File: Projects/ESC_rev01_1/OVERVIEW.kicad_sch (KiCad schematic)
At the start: 0 parts

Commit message: Update 07
Schematic is ready
INPUT PROTECTION schematic created
MOSFETs schematic created
CAN schematic created
FILTERs schematic created
MECHANICAL schematic created
STEP-DOWN schematic created
Footprints, 3D models are added and corrected (major issues)
Component placement started
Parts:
- added CR1: PUSB3AB6Z, DF_ESC_rev01_1:XSON-7_L2.2-W1.2-P0.50-BL, symbol PUSB3AB6Z:PUSB3AB6Z
- added R56, R57, R58: 0R, Resistor_SMD:R_0603_1608Metric, symbol Device:R
- added R59, R60: 5k1, Resistor_SMD:R_0603_1608Metric, symbol Device:R
- added R61, R62: 22R, Resistor_SMD:R_0603_1608Metric, symbol Device:R
- added U11: TYPE-C-31-M-12, DF_ESC_rev01_1:USB-C_SMD-TYPE-C-31-M-12_1, symbol TYPE-C-31-M-12:TYPE-C-31-M-12
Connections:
- new net: R56.2, R57.2, U11.1 (EH), U11.2 (EH), U11.3 (EH), U11.4 (EH)
- new net +5V: R58.2
- new net +5V-C: CR1.3 (IO2), CR1.5 (IO4), R58.1, U11.A4B9 (VBUS), U11.B4A9 (VBUS)
- new net CC1: CR1.4 (IO3), R60.2, U11.A5 (CC1)
- new net CC2: CR1.1 (IO1), R59.2, U11.B5 (CC2)
- new net GND: CR1.2 (GND), R56.1, R57.1, R59.1, R60.1, U11.A1B12 (GND), U11.B1A12 (GND)
- new net USB-C_N: CR1.6 (IO5), R61.1, U11.A7 (DN1), U11.B7 (DN2)
- new net USB-C_P: CR1.7 (IO6), R62.1, U11.A6 (DP1), U11.B6 (DP2)
- new net USB_N: R61.2
- new net USB_P: R62.2
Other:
- note added: "ESD PROTECTION PLACE AS CLOSE AS POSSIBLE TO THE CONNECTOR"
- note added: "FIT A ZERO OMH LINK, CAP, OR RESISTOR"
- note added: "MOUNT A OR JUMPER IF USED AS USB HOST"
- note added: "PULL-DOWN TELL THE HOST WE ARE UFP. ONLY ONE USED AT GIVEN TIME. BOTH NECESSARY FOR REVERSIBILITY."
- note added: "ROUTE AS DIFFERENTIAL PAIR"
- note added: "TERMINATING RESISTORS PLACE AS CLOSE AS POSSIBLE TO MCU"
- note added: "[09] - USB"

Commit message: Update 09
Components placement finished
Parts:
- renumbered U11 to J11, R56 to R53, R57 to R54, R58 to R55, R59 to R56, R60 to R57, R61 to R58, R62 to R59
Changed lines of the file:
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@@
 		(on_board yes)
 		(dnp no)
-		(property "Reference" "#PWR098"
+		(property "Reference" "#PWR095"
 			(at 100.33 142.24 0)
 			(effects
@@
 			(project "ESC_rev01_1"
 				(path "/e63e39d7-6ac0-4ffd-8aa3-1841a4541b55/aa28b6a5-844a-4eb8-af03-0b1ead627e2c"
-					(reference "#PWR098")
+					(reference "#PWR095")
 					(unit 1)
 				)
@@
 		(on_board yes)
 		(dnp no)
-		(property "Reference" "R58"
+		(property "Reference" "R55"
 			(at 128.778 70.104 0)
 			(effects
@@
 			(project "ESC_rev01_1"
 				(path "/e63e39d7-6ac0-4ffd-8aa3-1841a4541b55/aa28b6a5-844a-4eb8-af03-0b1ead627e2c"
-					(reference "R58")
+					(reference "R55")
 					(unit 1)
 				)
@@
 		(on_board yes)
 		(dnp no)
-		(property "Reference" "R61"
+		(property "Reference" "R58"
 			(at 203.2 71.12 90)
 			(effects
@@
 			(project "ESC_rev01_1"
 				(path "/e63e39d7-6ac0-4ffd-8aa3-1841a4541b55/aa28b6a5-844a-4eb8-af03-0b1ead627e2c"
-					(reference "R61")
+					(reference "R58")
 					(unit 1)
 				)
@@
 		(on_board yes)
 		(dnp no)
-		(property "Reference" "#PWR0102"
+		(property "Reference" "#PWR099"
 			(at 187.96 114.3 0)
 			(effects
@@
 			(project "ESC_rev01_1"
 				(path "/e63e39d7-6ac0-4ffd-8aa3-1841a4541b55/aa28b6a5-844a-4eb8-af03-0b1ead627e2c"
-					(reference "#PWR0102")
+					(reference "#PWR099")
 					(unit 1)
 				)
@@
 		(dnp no)
 		(fields_autoplaced yes)
-		(property "Reference" "U11"
+		(property "Reference" "J11"
 			(at 99.06 71.12 0)
 			(effects
@@
 			(project ""
 				(path "/e63e39d7-6ac0-4ffd-8aa3-1841a4541b55/aa28b6a5-844a-4eb8-af03-0b1ead627e2c"
-					(reference "U11")
+					(reference "J11")
 					(unit 1)
 				)
@@
 		(dnp no)
 		(fields_autoplaced yes)
-		(property "Reference" "#PWR099"
+		(property "Reference" "#PWR096"
 			(at 125.73 62.23 0)
 			(effects
@@
 			(project ""
 				(path "/e63e39d7-6ac0-4ffd-8aa3-1841a4541b55/aa28b6a5-844a-4eb8-af03-0b1ead627e2c"
-					(reference "#PWR099")
+					(reference "#PWR096")
 					(unit 1)
 				)
@@
 		(on_board yes)
 		(dnp no)
-		(property "Reference" "R60"
+		(property "Reference" "R57"
 			(at 151.638 91.694 0)
 			(effects
@@
 			(project "ESC_rev01_1"
 				(path "/e63e39d7-6ac0-4ffd-8aa3-1841a4541b55/aa28b6a5-844a-4eb8-af03-0b1ead627e2c"
-					(reference "R60")
+					(reference "R57")
 					(unit 1)
 				)
@@
 		(on_board yes)
 		(dnp no)
-		(property "Reference" "#PWR0100"
+		(property "Reference" "#PWR097"
 			(at 140.97 106.68 0)
 			(effects
@@
 			(project "ESC_rev01_1"
 				(path "/e63e39d7-6ac0-4ffd-8aa3-1841a4541b55/aa28b6a5-844a-4eb8-af03-0b1ead627e2c"
-					(reference "#PWR0100")
+					(reference "#PWR097")
 					(unit 1)
 				)
@@
 		(on_board yes)
 		(dnp no)
-		(property "Reference" "R59"
+		(property "Reference" "R56"
 			(at 144.018 91.694 0)
 			(effects
@@
 			(project "ESC_rev01_1"
 				(path "/e63e39d7-6ac0-4ffd-8aa3-1841a4541b55/aa28b6a5-844a-4eb8-af03-0b1ead627e2c"
-					(reference "R59")
+					(reference "R56")
 					(unit 1)
 				)
@@
 		(on_board yes)
 		(dnp no)
-		(property "Reference" "R56"
+		(property "Reference" "R53"
 			(at 88.138 124.714 0)
 			(effects
@@
 			(project "ESC_rev01_1"
 				(path "/e63e39d7-6ac0-4ffd-8aa3-1841a4541b55/aa28b6a5-844a-4eb8-af03-0b1ead627e2c"
-					(reference "R56")
+					(reference "R53")
 					(unit 1)
 				)
@@
 		(on_board yes)
 		(dnp no)
-		(property "Reference" "R62"
+		(property "Reference" "R59"
 			(at 203.2 77.47 90)
 			(effects
@@
 			(project "ESC_rev01_1"
 				(path "/e63e39d7-6ac0-4ffd-8aa3-1841a4541b55/aa28b6a5-844a-4eb8-af03-0b1ead627e2c"
-					(reference "R62")
+					(reference "R59")
 					(unit 1)
 				)
@@
 		(on_board yes)
 		(dnp no)
-		(property "Reference" "#PWR0101"
+		(property "Reference" "#PWR098"
 			(at 148.59 106.68 0)
 			(effects
@@
 			(project "ESC_rev01_1"
 				(path "/e63e39d7-6ac0-4ffd-8aa3-1841a4541b55/aa28b6a5-844a-4eb8-af03-0b1ead627e2c"
-					(reference "#PWR0101")
+					(reference "#PWR098")
 					(unit 1)
 				)
@@
 		(on_board yes)
 		(dnp no)
-		(property "Reference" "R57"
+		(property "Reference" "R54"
 			(at 94.488 124.714 0)
 			(effects
@@
 			(project "ESC_rev01_1"
 				(path "/e63e39d7-6ac0-4ffd-8aa3-1841a4541b55/aa28b6a5-844a-4eb8-af03-0b1ead627e2c"
-					(reference "R57")
-					(unit 1)
-				)
+					(reference "R54")
+					(unit 1)
+				)

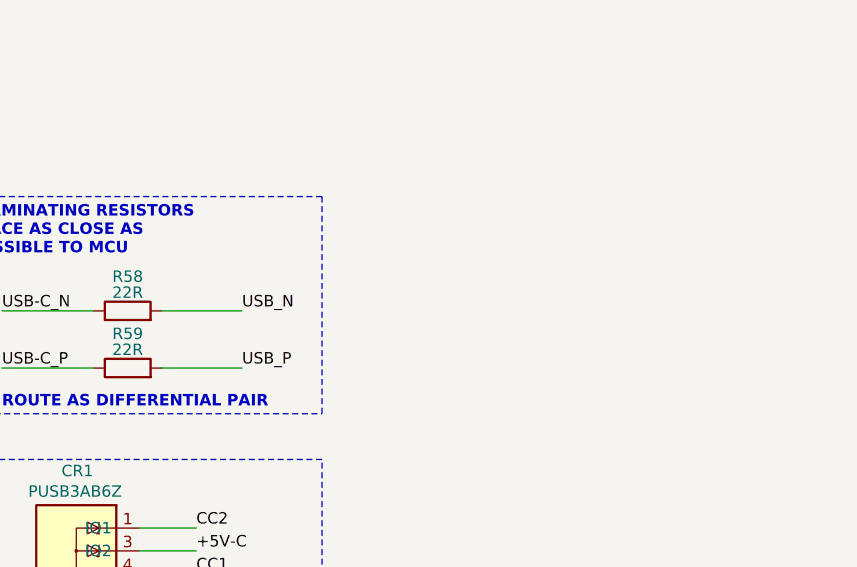
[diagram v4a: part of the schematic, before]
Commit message: Update 11
Draft routing - diff signals and power
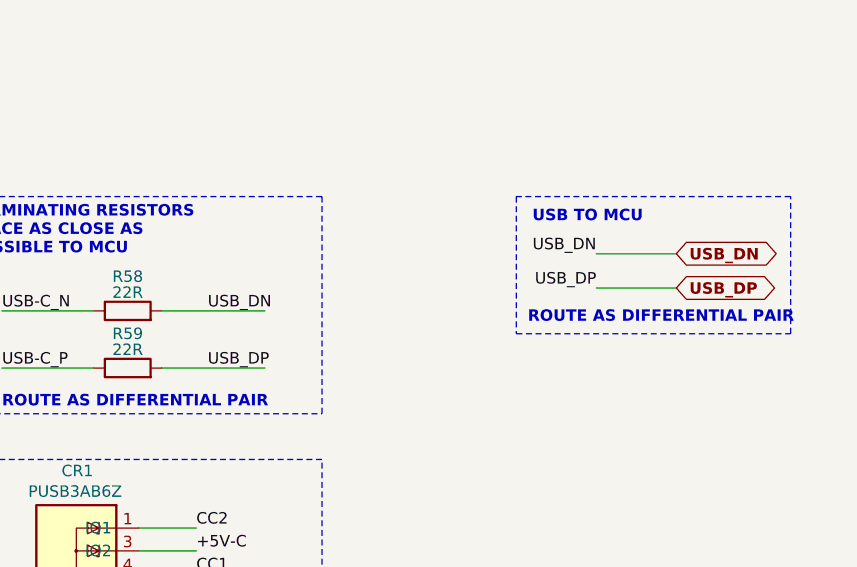
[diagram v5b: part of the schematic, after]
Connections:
- net USB_N renamed USB_DN
- net USB_P renamed USB_DP
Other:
- note added: "USB TO MCU"
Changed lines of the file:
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@@
+		)
+	)
+	(text "ROUTE AS DIFFERENTIAL PAIR"
+		(exclude_from_sim no)
+		(at 247.65 75.692 0)
+		(effects
+			(font
+				(size 1.27 1.27)
+				(thickness 0.254)
+				(bold yes)
+			)
+			(justify left)
 		)
 	)
@@
 		(exclude_from_sim no)
 		(at 100.33 64.77 0)
+		(effects
+			(font
+				(size 1.27 1.27)
+				(thickness 0.254)
+				(bold yes)
+			)
+			(justify left)
+		)
+	)
+	(text "USB TO MCU"
+		(exclude_from_sim no)
+		(at 248.158 64.516 0)
 		(effects
 			(font
@@
 		)
 	)
+	(polyline
+		(pts
+			(xy 246.38 62.23) (xy 246.38 77.47)
+		)
+		(stroke
+			(width 0)
+			(type dash)
+		)
+	)
+	(wire
+		(pts
+			(xy 264.16 68.58) (xy 255.27 68.58)
+		)
+		(stroke
+			(width 0.5)
+			(type default)
+		)
+	)
 	(wire
 		(pts
@@
 		)
 	)
+	(wire
+		(pts
+			(xy 207.01 81.28) (xy 218.44 81.28)
+		)
+		(stroke
+			(width 0.508)
+			(type default)
+		)
+	)
+	(polyline
+		(pts
+			(xy 276.86 77.47) (xy 276.86 62.23)
+		)
+		(stroke
+			(width 0)
+			(type dash)
+		)
+	)
 	(polyline
 		(pts
@@
 		)
 	)
-	(wire
-		(pts
-			(xy 215.9 81.28) (xy 207.01 81.28)
-		)
-		(stroke
-			(width 0.5)
-			(type default)
+	(polyline
+		(pts
+			(xy 246.38 77.47) (xy 276.86 77.47)
+		)
+		(stroke
+			(width 0)
+			(type dash)
 		)
 	)
@@
 	(wire
 		(pts
+			(xy 207.01 74.93) (xy 218.44 74.93)
+		)
+		(stroke
+			(width 0.508)
+			(type default)
+		)
+	)
+	(wire
+		(pts
 			(xy 91.44 133.35) (xy 100.33 133.35)
 		)
@@
 	(wire
 		(pts
+			(xy 264.16 72.39) (xy 255.27 72.39)
+		)
+		(stroke
+			(width 0.5)
+			(type default)
+		)
+	)
+	(wire
+		(pts
 			(xy 100.33 114.3) (xy 102.87 114.3)
 		)
@@
 		)
 	)
-	(wire
-		(pts
-			(xy 207.01 74.93) (xy 215.9 74.93)
-		)
-		(stroke
-			(width 0.5)
-			(type default)
-		)
-	)
 	(polyline
 		(pts
@@
 		)
 		(stroke
-			(width 0.5)
+			(width 0.508)
 			(type default)
 		)
@@
 		)
 		(stroke
-			(width 0.5)
+			(width 0.508)
 			(type default)
 		)
@@
 	(polyline
 		(pts
+			(xy 276.86 62.23) (xy 246.38 62.23)
+		)
+		(stroke
+			(width 0)
+			(type dash)
+		)
+	)
+	(polyline
+		(pts
 			(xy 100.33 68.58) (xy 100.33 60.96)
 		)
@@
 			(width 0)
 			(type default)
+		)
+	)
+	(label "USB_DN"
+		(at 212.09 74.93 0)
+		(effects
+			(font
+				(size 1.27 1.27)
+				(thickness 0.1588)
+			)
+			(justify left bottom)
 		)
 	)
@@
 		)
 	)
-	(label "USB_P"
-		(at 215.9 81.28 0)
-		(effects
-			(font
-				(size 1.27 1.27)
-			)
-			(justify left bottom)
+	(label "USB_DP"
+		(at 255.27 72.39 180)
+		(effects
+			(font
+				(size 1.27 1.27)
+			)
+			(justify right bottom)
 		)
 	)
@@
 		)
 	)
-	(label "USB_N"
-		(at 215.9 74.93 0)
-		(effects
-			(font
-				(size 1.27 1.27)
-			)
-			(justify left bottom)
+	(label "USB_DN"
+		(at 255.27 68.58 180)
+		(effects
+			(font
+				(size 1.27 1.27)
+			)
+			(justify right bottom)
 		)
 	)
@@
 		)
 	)
+	(label "USB_DP"
+		(at 212.09 81.28 0)
+		(effects
+			(font
+				(size 1.27 1.27)
+				(thickness 0.1588)
+			)
+			(justify left bottom)
+		)
+	)
 	(label "+5V-C"
 		(at 210.82 101.6 0)
@@
 		)
 	)
+	(global_label "USB_DP"
+		(shape bidirectional)
+		(at 264.16 72.39 0)
+		(fields_autoplaced yes)
+		(effects
+			(font
+				(size 1.27 1.27)
+				(thickness 0.254)
+				(bold yes)
+			)
+			(justify left)
+		)
+		(property "Intersheetrefs" "${INTERSHEET_REFS}"
+			(at 276.0499 72.39 0)
+			(effects
+				(font
+					(size 1.27 1.27)
+				)
+				(justify left)
+				(hide yes)
+			)
+		)
+	)
+	(global_label "USB_DN"
+		(shape bidirectional)
+		(at 264.16 68.58 0)
+		(fields_autoplaced yes)
+		(effects
+			(font
+				(size 1.27 1.27)
+				(thickness 0.254)
+				(bold yes)
+			)
+			(justify left)
+		)
+		(property "Intersheetrefs" "${INTERSHEET_REFS}"
+			(at 276.1104 68.58 0)
+			(effects
+				(font
+					(size 1.27 1.27)
+				)
+				(justify left)
+				(hide yes)
+			)
+		)
+	)

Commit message: Update 12
Continue routing
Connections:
- net USB-C_N: now also CR1.7 (IO6); no longer CR1.6 (IO5)
- net USB-C_P: now also CR1.6 (IO5); no longer CR1.7 (IO6)
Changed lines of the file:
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@@
-		)
-	)
-	(label "USB-C_P"
-		(at 210.82 111.76 0)
-		(effects
-			(font
-				(size 1.27 1.27)
-			)
-			(justify left bottom)
 		)
 	)
@@
 			)
 			(justify right bottom)
+		)
+	)
+	(label "USB-C_N"
+		(at 210.82 111.76 0)
+		(effects
+			(font
+				(size 1.27 1.27)
+			)
+			(justify left bottom)
 		)
 	)
@@
 		)
 	)
-	(label "USB-C_N"
-		(at 210.82 109.22 0)
-		(effects
-			(font
-				(size 1.27 1.27)
-			)
-			(justify left bottom)
-		)
-	)
 	(label "USB-C_P"
 		(at 123.19 100.33 0)
@@
 		(effects
 			(font
+				(size 1.27 1.27)
+			)
+			(justify left bottom)
+		)
+	)
+	(label "USB-C_P"
+		(at 210.82 109.22 0)
+		(effects
+			(font

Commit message: Update 01
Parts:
- CR1: footprint DF_ESC_rev01_1:XSON-7_L2.2-W1.2-P0.50-BL -> KeIr_lib:XSON-7_L2.2-W1.2-P0.50-BL
- J11: footprint DF_ESC_rev01_1:USB-C_SMD-TYPE-C-31-M-12_1 -> KeIr_lib:USB-C_SMD-TYPE-C-31-M-12_1
- R53, R54, R55: value 0R -> R
- R56, R57: value 5k1 -> R
- R58, R59: value 22R -> R
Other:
- title: (none) -> DF_ESC_rev01_1
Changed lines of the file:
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@@
 	(generator_version "9.0")
 	(paper "A4")
+	(title_block
+		(title "DF_ESC_rev01_1")
+		(rev "01_1")
+		(comment 1 "Irina Kenko")
+		(comment 3 "irkenk8@gmail.com")
+		(comment 4 "Irina Kenko")
+		(comment 5 "irkenk8@gmail.com")
+	)
 	(text "TERMINATING RESISTORS\nPLACE AS CLOSE AS\nPOSSIBLE TO MCU"
 		(exclude_from_sim no)
@@
 		(on_board yes)
 		(dnp no)
-		(property "Reference" "#PWR095"
+		(property "Reference" "#PWR94"
 			(at 100.33 142.24 0)
 			(effects
@@
 			(project "ESC_rev01_1"
 				(path "/e63e39d7-6ac0-4ffd-8aa3-1841a4541b55/aa28b6a5-844a-4eb8-af03-0b1ead627e2c"
-					(reference "#PWR095")
+					(reference "#PWR94")
 					(unit 1)
 				)
@@
 			)
 		)
-		(property "Value" "0R"
+		(property "Value" "R"
 			(at 128.27 71.882 0)
 			(effects
@@
 			)
 		)
-		(property "Footprint" "DF_ESC_rev01_1:XSON-7_L2.2-W1.2-P0.50-BL"
+		(property "Footprint" "KeIr_lib:XSON-7_L2.2-W1.2-P0.50-BL"
 			(at 195.58 105.41 0)
 			(effects
@@
 			)
 		)
-		(property "Value" "22R"
+		(property "Value" "R"
 			(at 203.2 72.898 90)
 			(effects
@@
 		(on_board yes)
 		(dnp no)
-		(property "Reference" "#PWR099"
+		(property "Reference" "#PWR98"
 			(at 187.96 114.3 0)
 			(effects
@@
 			(project "ESC_rev01_1"
 				(path "/e63e39d7-6ac0-4ffd-8aa3-1841a4541b55/aa28b6a5-844a-4eb8-af03-0b1ead627e2c"
-					(reference "#PWR099")
+					(reference "#PWR98")
 					(unit 1)
 				)
@@
 			)
 		)
-		(property "Footprint" "DF_ESC_rev01_1:USB-C_SMD-TYPE-C-31-M-12_1"
+		(property "Footprint" "KeIr_lib:USB-C_SMD-TYPE-C-31-M-12_1"
 			(at 99.06 102.87 0)
 			(effects
@@
 		(dnp no)
 		(fields_autoplaced yes)
-		(property "Reference" "#PWR096"
+		(property "Reference" "#PWR95"
 			(at 125.73 62.23 0)
 			(effects
@@
 			(project ""
 				(path "/e63e39d7-6ac0-4ffd-8aa3-1841a4541b55/aa28b6a5-844a-4eb8-af03-0b1ead627e2c"
-					(reference "#PWR096")
+					(reference "#PWR95")
 					(unit 1)
 				)
@@
 			)
 		)
-		(property "Value" "5k1"
+		(property "Value" "R"
 			(at 151.638 93.472 0)
 			(effects
@@
 		(on_board yes)
 		(dnp no)
-		(property "Reference" "#PWR097"
+		(property "Reference" "#PWR96"
 			(at 140.97 106.68 0)
 			(effects
@@
 			(project "ESC_rev01_1"
 				(path "/e63e39d7-6ac0-4ffd-8aa3-1841a4541b55/aa28b6a5-844a-4eb8-af03-0b1ead627e2c"
-					(reference "#PWR097")
+					(reference "#PWR96")
 					(unit 1)
 				)
@@
 			)
 		)
-		(property "Value" "5k1"
+		(property "Value" "R"
 			(at 144.018 93.472 0)
 			(effects
@@
 			)
 		)
-		(property "Value" "0R"
+		(property "Value" "R"
 			(at 87.63 126.492 0)
 			(effects
@@
 			)
 		)
-		(property "Value" "22R"
+		(property "Value" "R"
 			(at 203.2 79.248 90)
 			(effects
@@
 		(on_board yes)
 		(dnp no)
-		(property "Reference" "#PWR098"
+		(property "Reference" "#PWR97"
 			(at 148.59 106.68 0)
 			(effects
@@
 			(project "ESC_rev01_1"
 				(path "/e63e39d7-6ac0-4ffd-8aa3-1841a4541b55/aa28b6a5-844a-4eb8-af03-0b1ead627e2c"
-					(reference "#PWR098")
+					(reference "#PWR97")
 					(unit 1)
 				)
@@
 			)
 		)
-		(property "Value" "0R"
+		(property "Value" "R"
 			(at 93.98 126.492 0)
 			(effects
